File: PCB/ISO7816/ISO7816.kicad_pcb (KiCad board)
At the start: 2 copper layers, 68 x 81 mm, 54 parts, among them J1 Conn_01x02, J3 Conn_01x08, J4 Conn_01x08, J6 USB-C-Socket-H, J7 TC2030-USB-NL-DS, Q1 BSS138PS, Q2 BSS138PS, Q3 BSS138PS, Q4 BSS84, U1 ESP32-S3-MINI-1-N4R2, U2 SN74LVC1T45DCK, U3 TPS562246, U4 TPS22916CNYFPR, U5 TPS22916CNYFPR, U6 SN74LVC1T45DCK

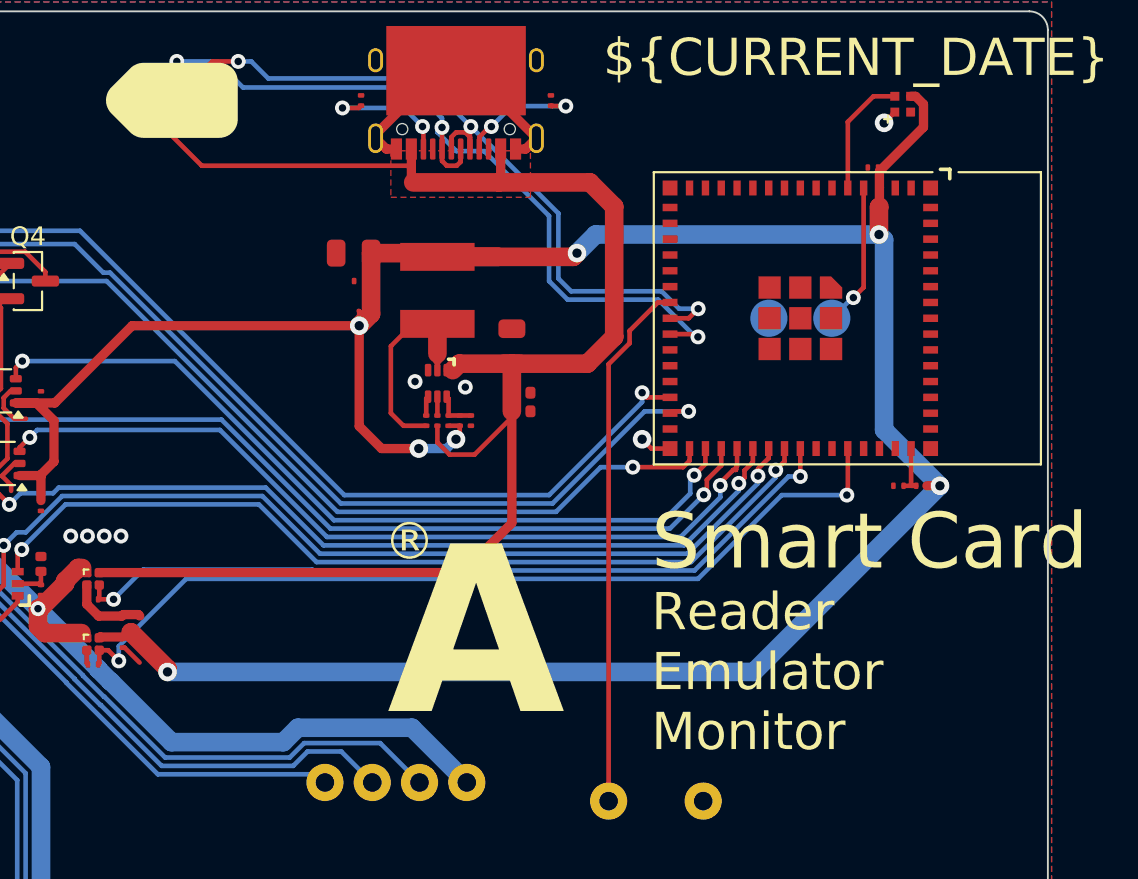
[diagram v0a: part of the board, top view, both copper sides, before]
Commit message: Added serial
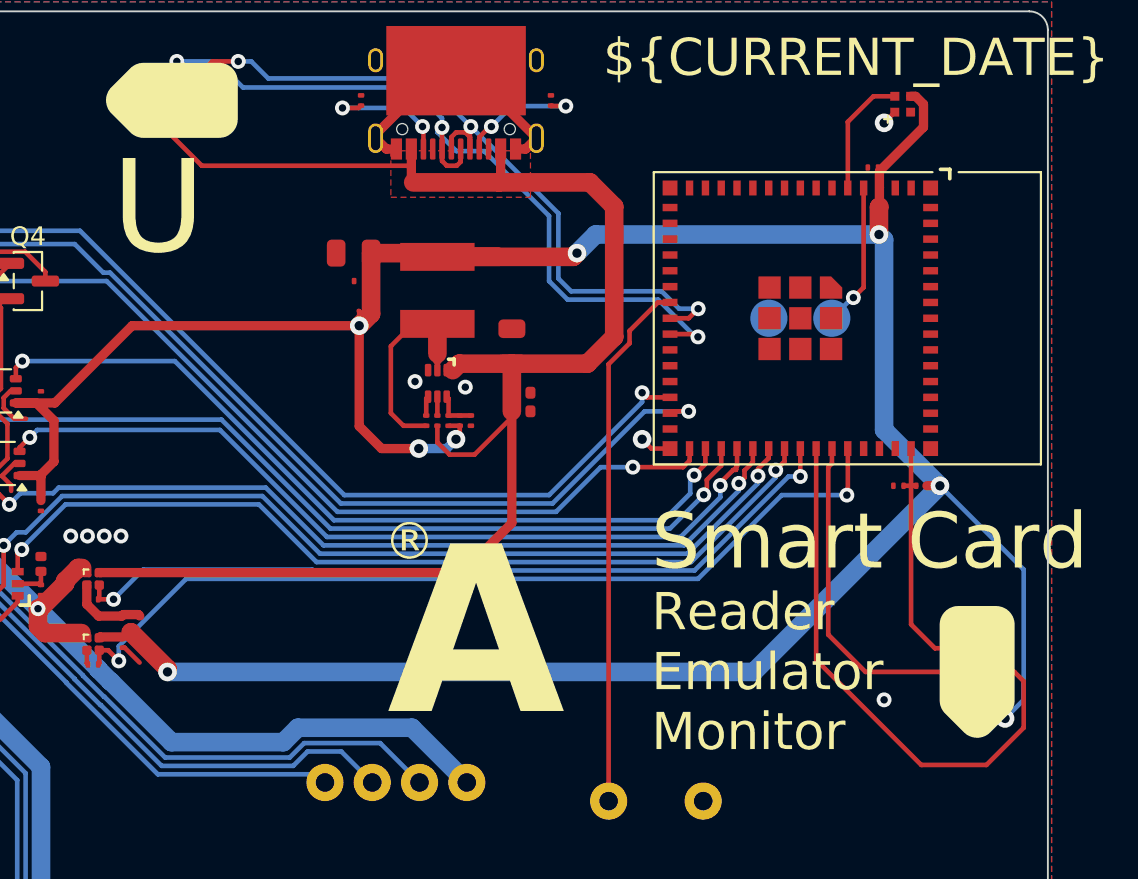
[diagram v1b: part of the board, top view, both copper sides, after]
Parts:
- added J8: TC2030-Serial-NL, RevK:Tag-Connect_TC2030-IDC-NL_2x03_P1.27mm_Vertical, F.Cu at (207.0, 108.5)
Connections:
- net Net-(U1-EN) renamed RTS
- U1 pad 39: unconnected-(U1-GPIO43-Pad39) -> TX
- U1 pad 40: unconnected-(U1-GPIO44-Pad40) -> RX
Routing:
- net TX: track 0.00 -> 30.2 mm
- net RX: track 0.00 -> 18.3 mm
- net +3.3V: track 151.2 -> 167.6 mm, vias 7 -> 8
- net RTS: track 2.70 -> 13.6 mm
- net GND: vias 13 -> 14
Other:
- board text added: "U"
